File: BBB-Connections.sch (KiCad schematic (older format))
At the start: 14 parts, among them P12 CONN_02X02, P13 JST_2, P8 CONN_23X2, P9 CONN_23X2

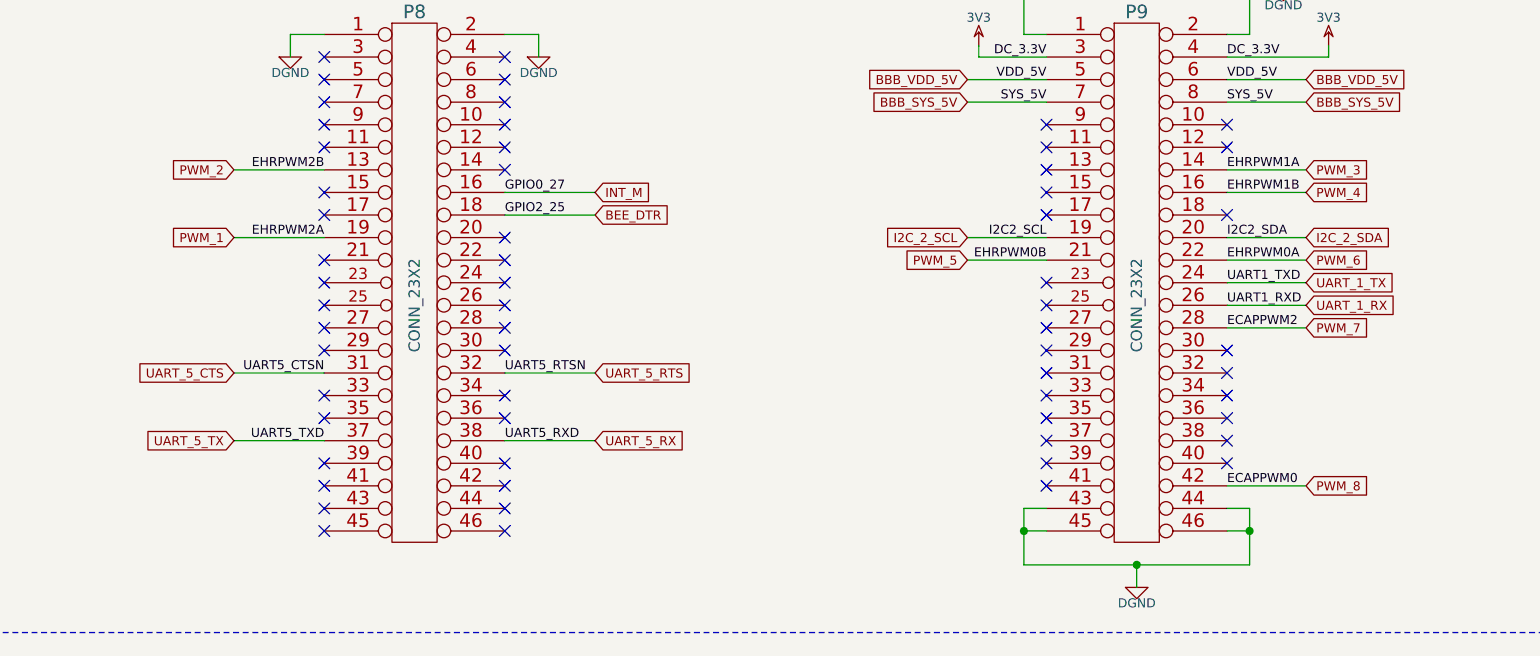
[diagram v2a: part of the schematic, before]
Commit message: layout in progress, corrected pwm order
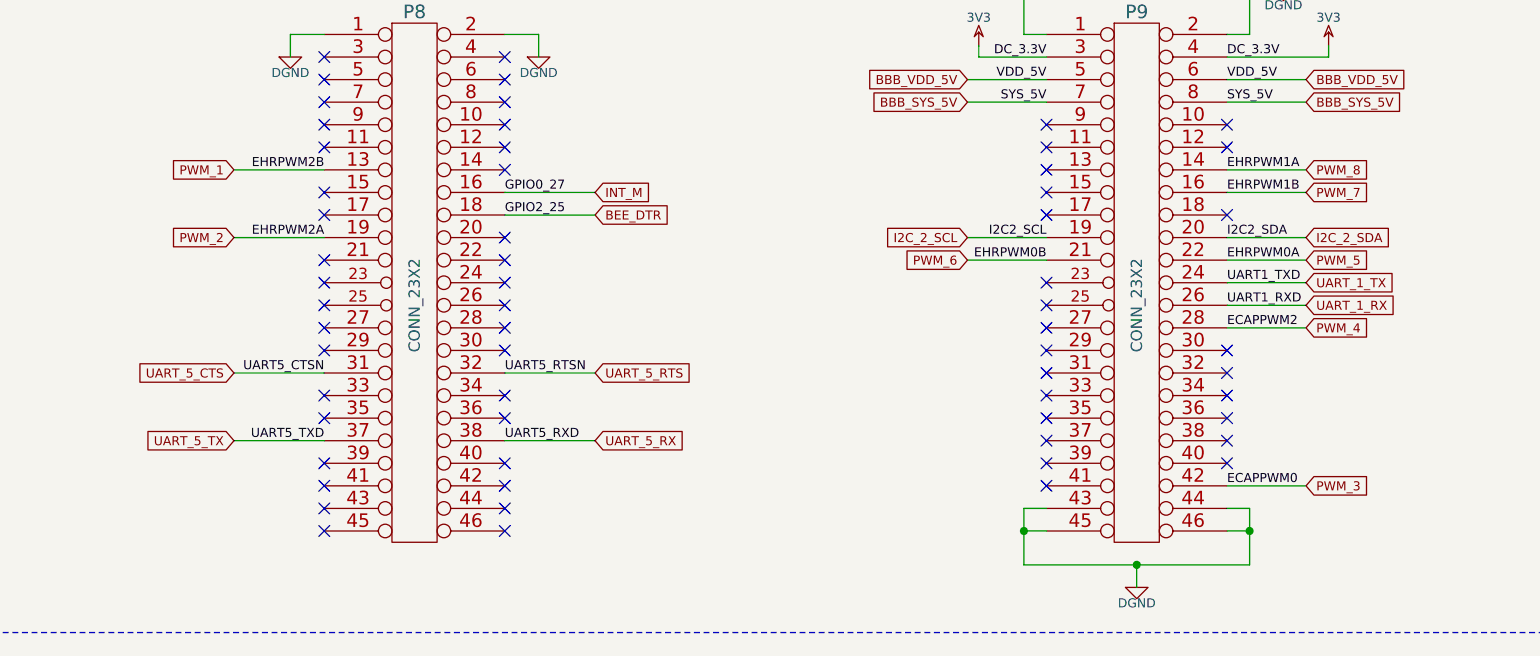
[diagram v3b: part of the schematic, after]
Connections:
- net PWM_1: now also P8.13 (P13); no longer P8.19 (P19)
- net PWM_2: now also P8.19 (P19); no longer P8.13 (P13)
- net PWM_3: now also P9.42 (P42); no longer P9.14 (P14)
- net PWM_4: now also P9.28 (P28); no longer P9.16 (P16)
- net PWM_5: now also P9.22 (P22); no longer P9.21 (P21)
- net PWM_6: now also P9.21 (P21); no longer P9.22 (P22)
- net PWM_7: now also P9.16 (P16); no longer P9.28 (P28)
- net PWM_8: now also P9.14 (P14); no longer P9.42 (P42)
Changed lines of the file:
@@
 Wire Wire Line
 	7800 2950 8150 2950
-Text GLabel 8150 3750 2    40   Input ~ 0
+Text GLabel 8150 2350 2    40   Input ~ 0
 PWM_8
 Wire Wire Line
@@
 Text Label 7800 3050 0    40   ~ 0
 ECAPPWM2
-Text GLabel 8150 3050 2    40   Input ~ 0
+Text GLabel 8150 2450 2    40   Input ~ 0
 PWM_7
 Wire Wire Line
 	8150 3050 7800 3050
-Text GLabel 8150 2750 2    40   Input ~ 0
+Text GLabel 6650 2750 0    40   Input ~ 0
 PWM_6
 Wire Wire Line
@@
 Text Label 7800 2350 0    40   ~ 0
 EHRPWM1A
-Text GLabel 8150 2350 2    40   Input ~ 0
+Text GLabel 8150 3750 2    40   Input ~ 0
 PWM_3
 Wire Wire Line
@@
 Text Label 7800 2450 0    40   ~ 0
 EHRPWM1B
-Text GLabel 8150 2450 2    40   Input ~ 0
+Text GLabel 8150 3050 2    40   Input ~ 0
 PWM_4
 Wire Wire Line
@@
 Text Label 3800 2650 2    40   ~ 0
 EHRPWM2A
-Text GLabel 3400 2650 0    40   Input ~ 0
+Text GLabel 3400 2350 0    40   Input ~ 0
 PWM_1
 Wire Wire Line
@@
 Text Label 3800 2350 2    40   ~ 0
 EHRPWM2B
-Text GLabel 3400 2350 0    40   Input ~ 0
+Text GLabel 3400 2650 0    40   Input ~ 0
 PWM_2
 Wire Wire Line
@@
 Text Label 7000 2750 2    40   ~ 0
 EHRPWM0B
-Text GLabel 6650 2750 0    40   Input ~ 0
+Text GLabel 8150 2750 2    40   Input ~ 0
 PWM_5
 Wire Wire Line

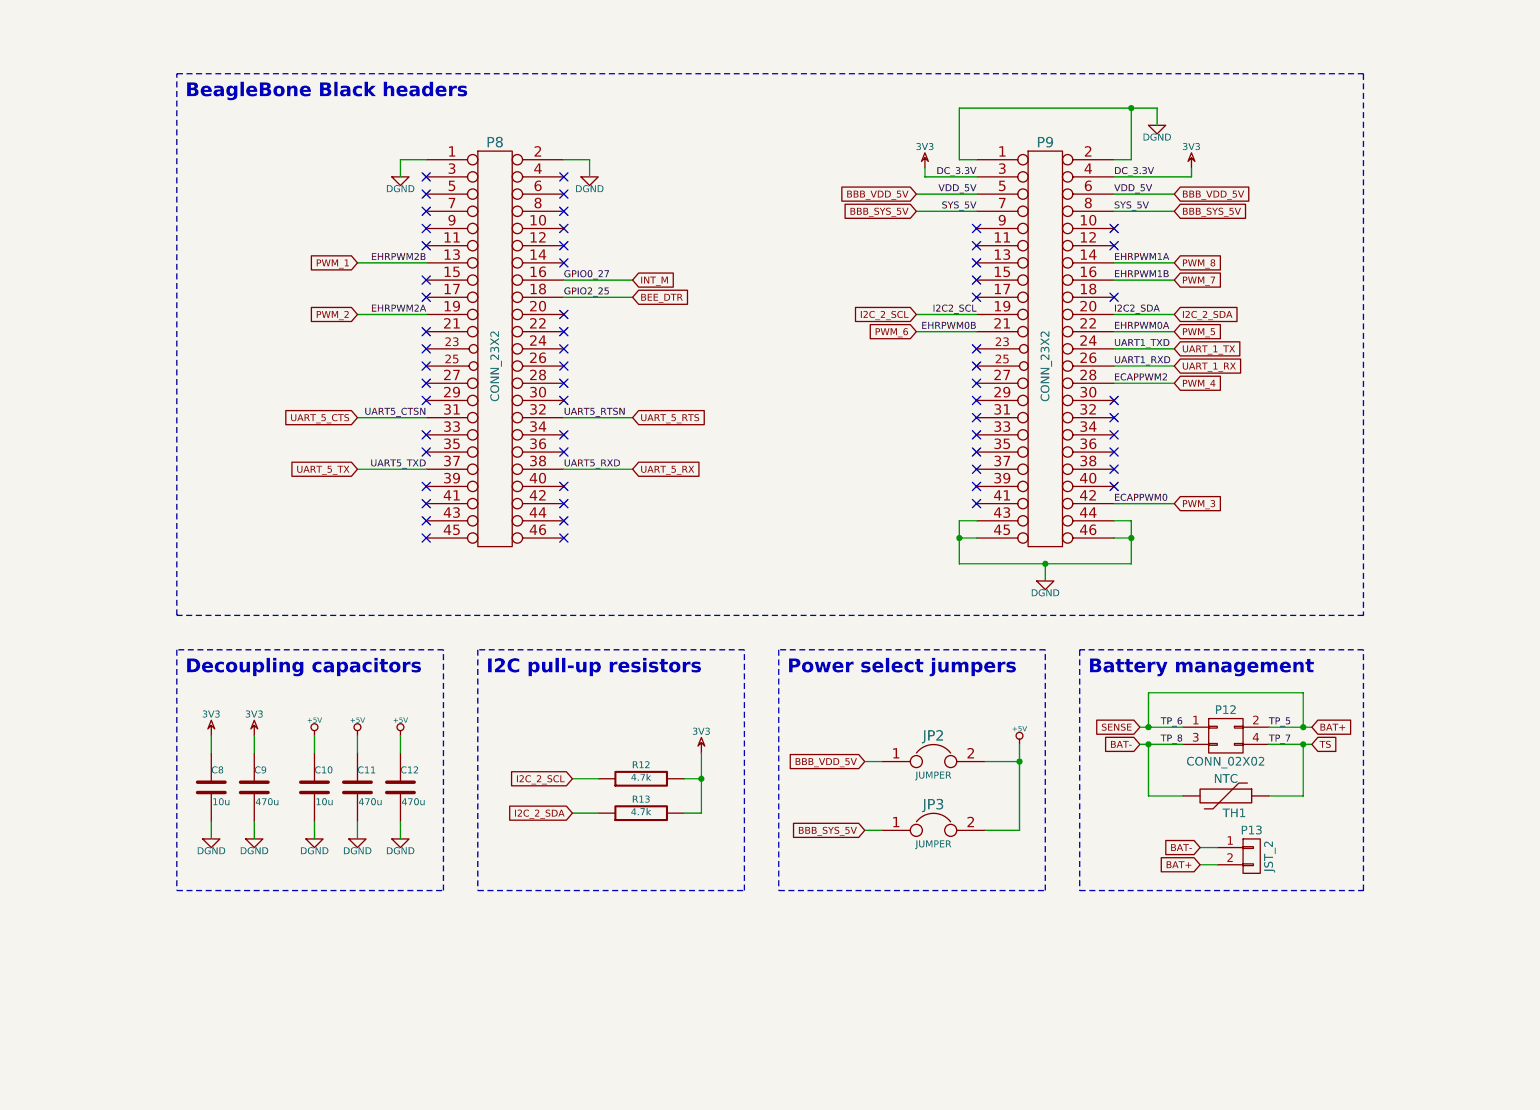
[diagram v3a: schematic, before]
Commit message: Added adc connectors w/ 5 to 1.8V conversion
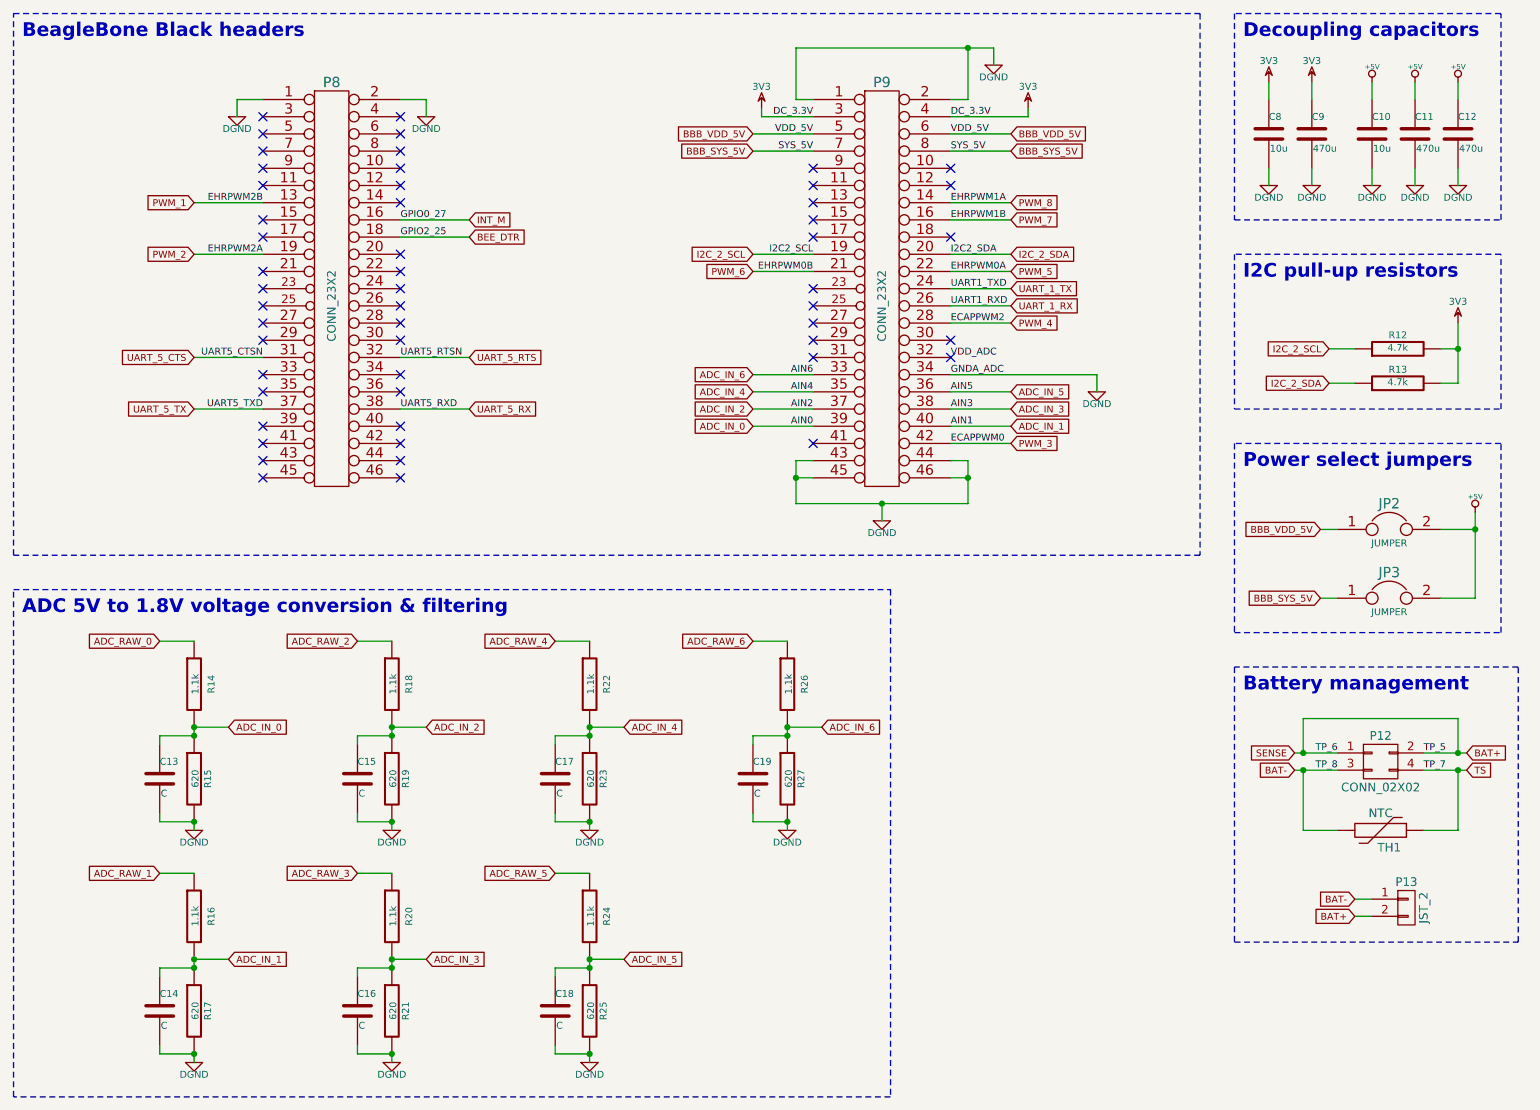
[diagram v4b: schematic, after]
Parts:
- added C13, C14, C15, C16, C17, C18, C19: C, symbol C
- added R14, R16, R18, R20, R22, R24, R26: 1.1k, symbol R
- added R15, R17, R19, R21, R23, R25, R27: 620, symbol R
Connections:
- net DGND: now also P9.34 (P34), C13.2, C14.2, C15.2, C16.2, C17.2, C18.2, C19.2, R15.2, R17.2, R19.2, R21.2, R23.2, R25.2, R27.2
- net VDD_ADC: now reaches P9.32 (P32)
- net ADC_IN_6: now reaches P9.33 (P33)
- net ADC_IN_6: now also C19.1, R26.2, R27.1
- net ADC_IN_4: now reaches P9.35 (P35)
- net ADC_IN_4: now also C17.1, R22.2, R23.1
- net ADC_IN_5: now reaches P9.36 (P36)
- net ADC_IN_5: now also C18.1, R24.2, R25.1
- net ADC_IN_2: now reaches P9.37 (P37)
- net ADC_IN_2: now also C15.1, R18.2, R19.1
- net ADC_IN_3: now reaches P9.38 (P38)
- net ADC_IN_3: now also C16.1, R20.2, R21.1
- net ADC_IN_0: now reaches P9.39 (P39)
- net ADC_IN_0: now also C13.1, R14.2, R15.1
- net ADC_IN_1: now reaches P9.40 (P40)
- net ADC_IN_1: now also C14.1, R16.2, R17.1
- new net ADC_RAW_0: R14.1
- new net ADC_RAW_1: R16.1
- new net ADC_RAW_2: R18.1
- new net ADC_RAW_3: R20.1
- new net ADC_RAW_4: R22.1
- new net ADC_RAW_5: R24.1
- new net ADC_RAW_6: R26.1
- no-connect marks 60 -> 52
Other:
- note added: "ADC 5V to 1.8V voltage conversion & filtering"
- moved on the sheet: C10, C11, C12, C8, C9, JP2, JP3, P12, P13, P8, P9, R12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

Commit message: Added comments on the schematics
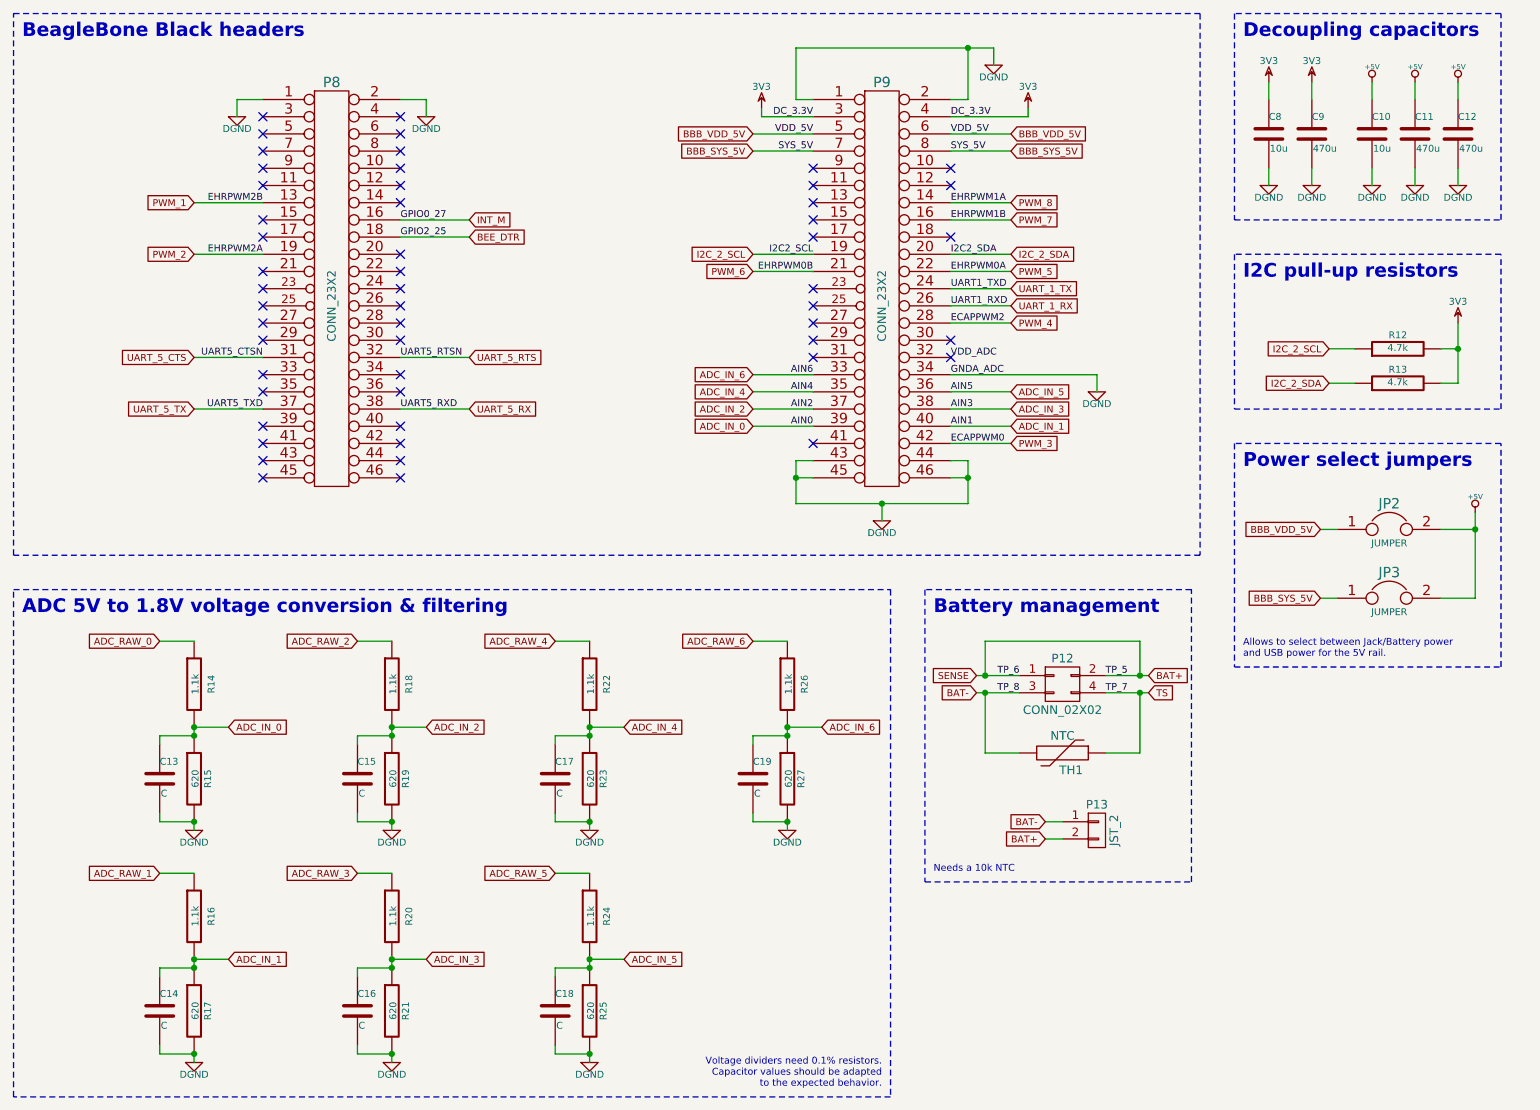
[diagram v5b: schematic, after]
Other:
- note added: "Allows to select between Jack/Battery power \nand USB power for the 5V rail."
- note added: "Needs a 10k NTC"
- note added: "Voltage dividers need 0.1% resistors.\nCapacitor values should be adapted\nto the expected behavior."
- moved on the sheet: P12, P13, TH1

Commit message: Update netlist & components footprints
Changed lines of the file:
@@
 	7100 1100 7100 1200
 Wire Wire Line
-	5950 1100 6950 1100
-Wire Wire Line
-	6950 1100 7100 1100
+	5950 1100 7100 1100
 Wire Wire Line
 	5950 1100 5950 1400
@@
 	6050 3600 5950 3600
 Wire Wire Line
-	5950 3500 5950 3600
+	5950 3500 5950 3750
 Wire Wire Line
-	5950 3600 5950 3750
-Wire Wire Line
-	6950 3750 6450 3750
-Wire Wire Line
-	6450 3750 5950 3750
+	6950 3750 5950 3750
 Wire Wire Line
 	6450 3750 6450 3850
 Wire Wire Line
-	6950 3500 6950 3600
-Wire Wire Line
-	6950 3600 6950 3750
+	6950 3500 6950 3750
 Wire Wire Line
 	6950 3600 6850 3600
@@
 	5700 2300 6050 2300
 Wire Wire Line
-	9800 2700 9800 2850
-Wire Wire Line
-	9800 2850 9800 3050
+	9800 2700 9800 3050
 Wire Wire Line
 	9800 2850 9700 2850
@@
 	5750 1500 6050 1500
 Wire Wire Line
-	9900 3800 9900 3900
-Wire Wire Line
-	9900 3900 9900 4300
+	9900 3800 9900 4300
 Wire Wire Line
 	9900 3900 9700 3900
@@
 	10050 3400 8500 3400
 Wire Wire Line
-	7750 4750 7950 4750
+	7750 4750 8000 4750
 Wire Wire Line
-	7950 4750 8000 4750
-Wire Wire Line
-	7000 4850 7050 4850
-Wire Wire Line
-	7050 4850 7250 4850
+	7000 4850 7250 4850
 Wire Wire Line
 	7400 5600 7500 5600
@@
 	7400 5700 7500 5700
 Wire Wire Line
-	7000 4750 7050 4750
-Wire Wire Line
-	7050 4750 7250 4750
+	7000 4750 7250 4750
 Wire Wire Line
 	7050 4750 7050 4550
@@
 	7950 5200 7950 4850
 Wire Wire Line
-	7750 4850 7950 4850
-Wire Wire Line
-	7950 4850 8000 4850
+	7750 4850 8000 4850
 Connection ~ 7950 4850
 Connection ~ 7050 4750

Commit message: Place components on PCB & ajust nets to stay w/ 2 layers
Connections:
- net ADC_IN_0: now also C18.1, R24.2, R25.1; no longer C13.1, R14.2, R15.1
- net ADC_IN_1: now also C19.1, R26.2, R27.1; no longer C14.1, R16.2, R17.1
- net ADC_IN_2: now also C16.1, R20.2, R21.1; no longer C15.1, R18.2, R19.1
- net ADC_IN_3: now also C17.1, R22.2, R23.1; no longer C16.1, R20.2, R21.1
- net ADC_IN_4: now also C14.1, R16.2, R17.1; no longer C17.1, R22.2, R23.1
- net ADC_IN_5: now also C15.1, R18.2, R19.1; no longer C18.1, R24.2, R25.1
- net ADC_IN_6: now also C13.1, R14.2, R15.1; no longer C19.1, R26.2, R27.1
- net ADC_RAW_0: now also R24.1; no longer R14.1
- net ADC_RAW_1: now also R26.1; no longer R16.1
- net ADC_RAW_2: now also R20.1; no longer R18.1
- net ADC_RAW_3: now also R22.1; no longer R20.1
- net ADC_RAW_4: now also R16.1; no longer R22.1
- net ADC_RAW_5: now also R18.1; no longer R24.1
- net ADC_RAW_6: now also R14.1; no longer R26.1
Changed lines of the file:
@@
 Battery management
 NoConn ~ 6850 2800
-Text GLabel 2250 4550 0    40   Input ~ 0
+Text GLabel 4550 5900 0    40   Input ~ 0
 ADC_RAW_0
 $Comp
@@
 	1    0    0    -1
 $EndComp
-Text GLabel 2650 5050 2    40   Input ~ 0
+Text GLabel 4950 6400 2    40   Input ~ 0
 ADC_IN_0
 Text GLabel 5700 3300 0    40   Input ~ 0
@@
 Connection ~ 2450 5100
 Connection ~ 2450 5600
-Text GLabel 3400 4550 0    40   Input ~ 0
+Text GLabel 3400 5900 0    40   Input ~ 0
 ADC_RAW_2
 $Comp
@@
 	1    0    0    -1
 $EndComp
-Text GLabel 3800 5050 2    40   Input ~ 0
+Text GLabel 3800 6400 2    40   Input ~ 0
 ADC_IN_2
 $Comp
@@
 Connection ~ 3600 5100
 Connection ~ 3600 5600
-Text GLabel 4550 4550 0    40   Input ~ 0
+Text GLabel 2250 5900 0    40   Input ~ 0
 ADC_RAW_4
 $Comp
@@
 	1    0    0    -1
 $EndComp
-Text GLabel 4950 5050 2    40   Input ~ 0
+Text GLabel 2650 6400 2    40   Input ~ 0
 ADC_IN_4
 $Comp
@@
 Connection ~ 4750 5100
 Connection ~ 4750 5600
-Text GLabel 5700 4550 0    40   Input ~ 0
+Text GLabel 2250 4550 0    40   Input ~ 0
 ADC_RAW_6
 $Comp
@@
 	1    0    0    -1
 $EndComp
-Text GLabel 6100 5050 2    40   Input ~ 0
+Text GLabel 2650 5050 2    40   Input ~ 0
 ADC_IN_6
 $Comp
@@
 Connection ~ 5900 5100
 Connection ~ 5900 5600
-Text GLabel 2250 5900 0    40   Input ~ 0
+Text GLabel 5700 4550 0    40   Input ~ 0
 ADC_RAW_1
 $Comp
@@
 	1    0    0    -1
 $EndComp
-Text GLabel 2650 6400 2    40   Input ~ 0
+Text GLabel 6100 5050 2    40   Input ~ 0
 ADC_IN_1
 $Comp
@@
 Connection ~ 2450 6450
 Connection ~ 2450 6950
-Text GLabel 3400 5900 0    40   Input ~ 0
+Text GLabel 4550 4550 0    40   Input ~ 0
 ADC_RAW_3
 $Comp
@@
 	1    0    0    -1
 $EndComp
-Text GLabel 3800 6400 2    40   Input ~ 0
+Text GLabel 4950 5050 2    40   Input ~ 0
 ADC_IN_3
 $Comp
@@
 Connection ~ 3600 6450
 Connection ~ 3600 6950
-Text GLabel 4550 5900 0    40   Input ~ 0
+Text GLabel 3400 4550 0    40   Input ~ 0
 ADC_RAW_5
 $Comp
@@
 Connection ~ 4750 6450
 Connection ~ 4750 6950
-Text GLabel 4950 6400 2    40   Input ~ 0
+Text GLabel 3800 5050 2    40   Input ~ 0
 ADC_IN_5
 Text Notes 1450 4400 0    80   ~ 16
